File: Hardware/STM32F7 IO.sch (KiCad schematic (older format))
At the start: 33 parts, among them U4 STM32F765ZGT6, Y1 32.768kHz, Y2 8MHz

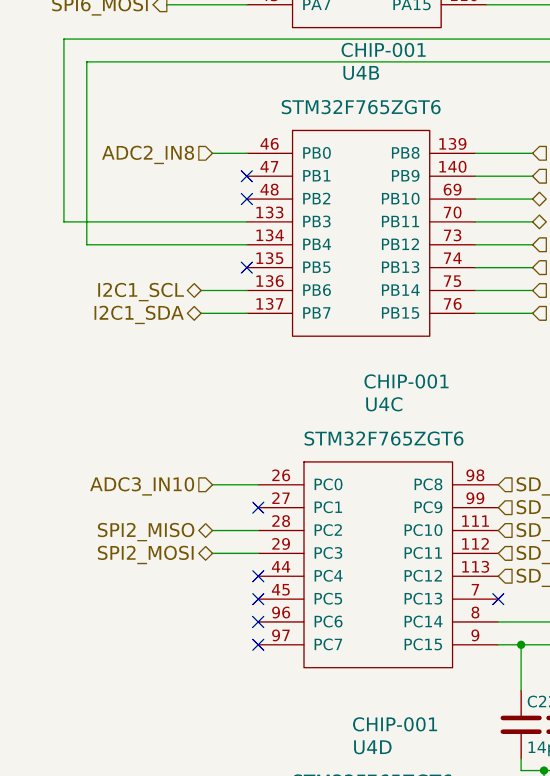
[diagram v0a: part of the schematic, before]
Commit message: Added additional headers to some interfaces, GPIOs, and FTDI pins. Added silks
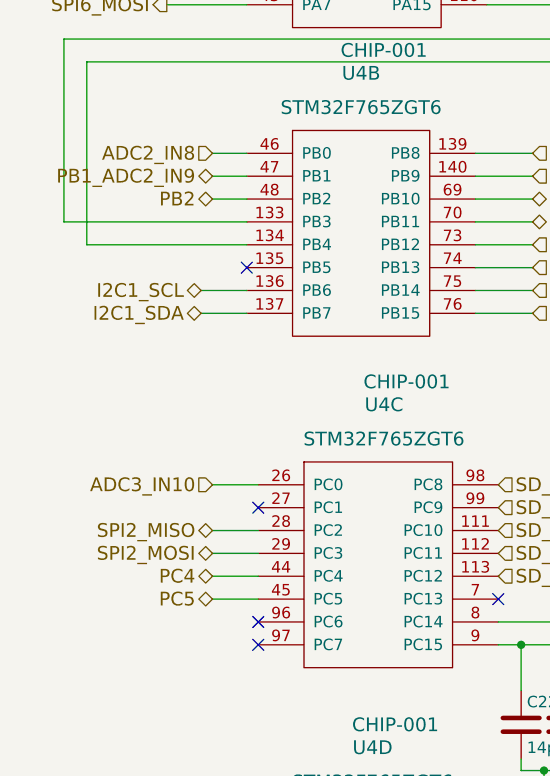
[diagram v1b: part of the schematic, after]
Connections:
- net PB1_ADC2_IN9: now reaches U4.47 (PB1)
- net PB2: now reaches U4.48 (PB2)
- net PC4: now reaches U4.44 (PC4)
- net PC5: now reaches U4.45 (PC5)
- no-connect marks 51 -> 47
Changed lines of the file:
@@
 $Descr A4 11693 8268
 encoding utf-8
-Sheet 3 10
+Sheet 10 10
 Title "Autopilot Controller I/O"
 Date "2017-05-14"
@@
 Text HLabel 7950 3200 2    60   BiDi ~ 0
 SPI5_NSS
-Text HLabel 1500 4600 0    60   BiDi ~ 0
-SPI2_MISO
-Text HLabel 1500 4700 0    60   BiDi ~ 0
-SPI2_MOSI
 Text HLabel 2900 3650 2    60   Input ~ 0
 UART4_CTS
@@
 MEM_WC
 NoConn ~ 1650 3450
-NoConn ~ 1650 3150
-NoConn ~ 1700 4800
-NoConn ~ 1700 4900
 NoConn ~ 2750 6200
 NoConn ~ 1700 6200
@@
 $Comp
 L WARG:STM32F765ZGT6 U4
-U 2 1 595F8A92
-P 2150 3500
-F 0 "U4" H 2150 4400 60  0000 C CNN
-F 1 "STM32F765ZGT6" H 2150 4250 60  0000 C CNN
-F 2 "Package_QFP:LQFP-144_20x20mm_P0.5mm" H 3200 3600 60  0001 C CNN
-F 3 "http://www.st.com/content/ccc/resource/technical/document/datasheet/group3/c5/37/9c/1d/a6/09/4e/1a/DM00273119/files/DM00273119.pdf/jcr:content/translations/en.DM00273119.pdf" H 3200 3600 60  0001 C CNN
-F 4 "CHIP-001" H 2250 4500 60  0000 C CNN "part_num"
-	2    2150 3500
-	1    0    0    -1
-$EndComp
-$Comp
-L WARG:STM32F765ZGT6 U4
-U 3 1 595F8B04
-P 2250 4950
-F 0 "U4" H 2250 5850 60  0000 C CNN
-F 1 "STM32F765ZGT6" H 2250 5700 60  0000 C CNN
-F 2 "Package_QFP:LQFP-144_20x20mm_P0.5mm" H 3300 5050 60  0001 C CNN
-F 3 "http://www.st.com/content/ccc/resource/technical/document/datasheet/group3/c5/37/9c/1d/a6/09/4e/1a/DM00273119/files/DM00273119.pdf/jcr:content/translations/en.DM00273119.pdf" H 3300 5050 60  0001 C CNN
-F 4 "CHIP-001" H 2350 5950 60  0000 C CNN "part_num"
-	3    2250 4950
-	1    0    0    -1
-$EndComp
-$Comp
-L WARG:STM32F765ZGT6 U4
 U 5 1 595F8BE2
 P 6500 2000
@@
 Wire Wire Line
 	1500 2950 1650 2950
-Wire Wire Line
-	1700 4700 1500 4700
-Wire Wire Line
-	1700 4600 1500 4600
 Wire Wire Line
 	5850 3500 6050 3500
@@
 	1300 2300 1650 2300
 NoConn ~ 1700 4500
-NoConn ~ 1650 3050
+$Comp
+L WARG:STM32F765ZGT6 U4
+U 3 1 595F8B04
+P 2250 4950
+F 0 "U4" H 2250 5850 60  0000 C CNN
+F 1 "STM32F765ZGT6" H 2250 5700 60  0000 C CNN
+F 2 "Package_QFP:LQFP-144_20x20mm_P0.5mm" H 3300 5050 60  0001 C CNN
+F 3 "http://www.st.com/content/ccc/resource/technical/document/datasheet/group3/c5/37/9c/1d/a6/09/4e/1a/DM00273119/files/DM00273119.pdf/jcr:content/translations/en.DM00273119.pdf" H 3300 5050 60  0001 C CNN
+F 4 "CHIP-001" H 2350 5950 60  0000 C CNN "part_num"
+	3    2250 4950
+	1    0    0    -1
+$EndComp
+Wire Wire Line
+	1700 4800 1500 4800
+Wire Wire Line
+	1500 4900 1700 4900
+$Comp
+L WARG:STM32F765ZGT6 U4
+U 2 1 595F8A92
+P 2150 3500
+F 0 "U4" H 2150 4400 60  0000 C CNN
+F 1 "STM32F765ZGT6" H 2150 4250 60  0000 C CNN
+F 2 "Package_QFP:LQFP-144_20x20mm_P0.5mm" H 3200 3600 60  0001 C CNN
+F 3 "http://www.st.com/content/ccc/resource/technical/document/datasheet/group3/c5/37/9c/1d/a6/09/4e/1a/DM00273119/files/DM00273119.pdf/jcr:content/translations/en.DM00273119.pdf" H 3200 3600 60  0001 C CNN
+F 4 "CHIP-001" H 2250 4500 60  0000 C CNN "part_num"
+	2    2150 3500
+	1    0    0    -1
+$EndComp
+Wire Wire Line
+	1650 3050 1500 3050
+Text HLabel 1500 4800 0    60   BiDi ~ 0
+PC4
+Text HLabel 1500 4900 0    60   BiDi ~ 0
+PC5
+Text HLabel 1500 3050 0    60   BiDi ~ 0
+PB1_ADC2_IN9
+Wire Wire Line
+	1650 3150 1500 3150
+Text HLabel 1500 3150 0    60   BiDi ~ 0
+PB2
+Wire Wire Line
+	1700 4600 1500 4600
+Wire Wire Line
+	1500 4700 1700 4700
+Text HLabel 1500 4600 0    60   BiDi ~ 0
+SPI2_MISO
+Text HLabel 1500 4700 0    60   BiDi ~ 0
+SPI2_MOSI
 $EndSCHEMATC

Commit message: associated components to their JLC part numbers
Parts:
- C22, C23: LCSC (none) -> C1644
- C24, C25, C26, C27, C28, C29, C30, C31, C33, C34, C35, C36: LCSC (none) -> C14663
- C32, C37: LCSC (none) -> C15849
- C38: LCSC (none) -> C19666
- C39, C40: LCSC (none) -> C1679
- C41, C42: LCSC (none) -> C23630
- D5, D6, D7: LCSC (none) -> C72043
- R16, R17, R18: LCSC (none) -> C22775
- R19: LCSC (none) -> C25804
- R20: LCSC (none) -> C21189
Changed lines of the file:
@@
 EESchema Schematic File Version 4
-LIBS:ZP-Breakout-cache
-EELAYER 29 0
+EELAYER 30 0
 EELAYER END
 $Descr A4 11693 8268
@@
 F 3 "https://ds.yuden.co.jp/TYCOMPAS/ut/specSheet?pn=TMK107ABJ225KA-T++" H 10350 5550 50  0001 C CNN
 F 4 "CAPP-007" H 10350 5550 60  0001 C CNN "part_num"
+F 5 "C23630" H 10350 5550 50  0001 C CNN "LCSC"
 	1    10350 5550
 	0    1    1    0
@@
 F 3 "https://ds.yuden.co.jp/TYCOMPAS/ut/specSheet?pn=TMK107ABJ225KA-T++" H 10350 5850 50  0001 C CNN
 F 4 "CAPP-007" H 10350 5850 60  0001 C CNN "part_num"
+F 5 "C23630" H 10350 5850 50  0001 C CNN "LCSC"
 	1    10350 5850
 	0    1    1    0
@@
 F 3 "https://search.murata.co.jp/Ceramy/image/img/A01X/G101/ENG/GRM188R71E104KA01-01.pdf" H 6350 4950 50  0001 C CNN
 F 4 "CAPP-005" H 6350 4950 60  0001 C CNN "part_num"
+F 5 "C14663" H 6350 4950 50  0001 C CNN "LCSC"
 	1    6350 4950
 	1    0    0    -1
@@
 F 3 "http://www.samsungsem.com/kr/support/product-search/mlcc/CL10A475MP5LNNC.jsp" H 8300 4950 50  0001 C CNN
 F 4 "CAPP-006" H 8300 4950 60  0001 C CNN "part_num"
+F 5 "C19666" H 8300 4950 50  0001 C CNN "LCSC"
 	1    8300 4950
 	1    0    0    1
@@
 F 3 "https://search.murata.co.jp/Ceramy/image/img/A01X/G101/ENG/GRM188R61E105KA12-01.pdf" H 7400 5700 50  0001 C CNN
 F 4 "CAPP-004" H 7400 5700 60  0001 C CNN "part_num"
+F 5 "C15849" H 7400 5700 50  0001 C CNN "LCSC"
 	1    7400 5700
 	1    0    0    1
@@
 F 3 "http://optoelectronics.liteon.com/upload/download/DS22-2000-228/LTST-C191KGKT.PDF" H 7850 1900 50  0001 C CNN
 F 4 "DIOD-002" H 7850 1900 60  0001 C CNN "part_num"
+F 5 "C72043" H 7850 1900 50  0001 C CNN "LCSC"
 	1    7850 1900
 	0    -1   -1   0
@@
 F 3 "http://optoelectronics.liteon.com/upload/download/DS22-2000-228/LTST-C191KGKT.PDF" H 8100 1900 50  0001 C CNN
 F 4 "DIOD-002" H 8100 1900 60  0001 C CNN "part_num"
+F 5 "C72043" H 8100 1900 50  0001 C CNN "LCSC"
 	1    8100 1900
 	0    -1   -1   0
@@
 F 3 "http://optoelectronics.liteon.com/upload/download/DS22-2000-228/LTST-C191KGKT.PDF" H 7600 1900 50  0001 C CNN
 F 4 "DIOD-002" H 7600 1900 60  0001 C CNN "part_num"
+F 5 "C72043" H 7600 1900 50  0001 C CNN "LCSC"
 	1    7600 1900
 	0    -1   -1   0
@@
 F 3 "http://www.yageo.com/documents/recent/PYu-RC_Group_51_RoHS_L_10.pdf" H 7600 2250 50  0001 C CNN
 F 4 "RESS-006" V 7600 2250 60  0001 C CNN "part_num"
+F 5 "C22775" V 7600 2250 50  0001 C CNN "LCSC"
 	1    7600 2250
 	1    0    0    -1
@@
 F 3 "http://www.yageo.com/documents/recent/PYu-RC_Group_51_RoHS_L_10.pdf" H 7850 2250 50  0001 C CNN
 F 4 "RESS-006" V 7850 2250 60  0001 C CNN "part_num"
+F 5 "C22775" V 7850 2250 50  0001 C CNN "LCSC"
 	1    7850 2250
 	1    0    0    -1
@@
 F 3 "http://www.yageo.com/documents/recent/PYu-RC_Group_51_RoHS_L_10.pdf" H 8100 2250 50  0001 C CNN
 F 4 "RESS-006" V 8100 2250 60  0001 C CNN "part_num"
+F 5 "C22775" V 8100 2250 50  0001 C CNN "LCSC"
 	1    8100 2250
 	1    0    0    -1
@@
 F 3 "https://search.murata.co.jp/Ceramy/image/img/A01X/G101/ENG/GRM188R61E105KA12-01.pdf" H 8100 5900 50  0001 C CNN
 F 4 "CAPP-004" H 8100 5900 60  0001 C CNN "part_num"
+F 5 "C15849" H 8100 5900 50  0001 C CNN "LCSC"
 	1    8100 5900
 	1    0    0    1
@@
 F 3 "https://search.murata.co.jp/Ceramy/image/img/A01X/G101/ENG/GRM188R71E104KA01-01.pdf" H 7800 5900 50  0001 C CNN
 F 4 "CAPP-005" H 7800 5900 60  0001 C CNN "part_num"
+F 5 "C14663" H 7800 5900 50  0001 C CNN "LCSC"
 	1    7800 5900
 	1    0    0    -1
@@
 F 3 "https://search.murata.co.jp/Ceramy/image/img/A01X/G101/ENG/GRM188R71E104KA01-01.pdf" H 7100 5700 50  0001 C CNN
 F 4 "CAPP-005" H 7100 5700 60  0001 C CNN "part_num"
+F 5 "C14663" H 7100 5700 50  0001 C CNN "LCSC"
 	1    7100 5700
 	1    0    0    -1
@@
 F 3 "https://search.murata.co.jp/Ceramy/image/img/A01X/G101/ENG/GRM188R71E104KA01-01.pdf" H 6550 4950 50  0001 C CNN
 F 4 "CAPP-005" H 6550 4950 60  0001 C CNN "part_num"
+F 5 "C14663" H 6550 4950 50  0001 C CNN "LCSC"
 	1    6550 4950
 	1    0    0    -1
@@
 F 3 "https://search.murata.co.jp/Ceramy/image/img/A01X/G101/ENG/GRM188R71E104KA01-01.pdf" H 6750 4950 50  0001 C CNN
 F 4 "CAPP-005" H 6750 4950 60  0001 C CNN "part_num"
+F 5 "C14663" H 6750 4950 50  0001 C CNN "LCSC"
 	1    6750 4950
 	1    0    0    -1
@@
 F 3 "https://search.murata.co.jp/Ceramy/image/img/A01X/G101/ENG/GRM188R71E104KA01-01.pdf" H 6950 4950 50  0001 C CNN
 F 4 "CAPP-005" H 6950 4950 60  0001 C CNN "part_num"
+F 5 "C14663" H 6950 4950 50  0001 C CNN "LCSC"
 	1    6950 4950
 	1    0    0    -1
@@
 F 3 "https://search.murata.co.jp/Ceramy/image/img/A01X/G101/ENG/GRM188R71E104KA01-01.pdf" H 7150 4950 50  0001 C CNN
 F 4 "CAPP-005" H 7150 4950 60  0001 C CNN "part_num"
+F 5 "C14663" H 7150 4950 50  0001 C CNN "LCSC"
 	1    7150 4950
 	1    0    0    -1
@@
 F 3 "https://search.murata.co.jp/Ceramy/image/img/A01X/G101/ENG/GRM188R71E104KA01-01.pdf" H 7350 4950 50  0001 C CNN
 F 4 "CAPP-005" H 7350 4950 60  0001 C CNN "part_num"
+F 5 "C14663" H 7350 4950 50  0001 C CNN "LCSC"
 	1    7350 4950
 	1    0    0    -1
@@
 F 3 "https://search.murata.co.jp/Ceramy/image/img/A01X/G101/ENG/GRM188R71E104KA01-01.pdf" H 7550 4950 50  0001 C CNN
 F 4 "CAPP-005" H 7550 4950 60  0001 C CNN "part_num"
+F 5 "C14663" H 7550 4950 50  0001 C CNN "LCSC"
 	1    7550 4950
 	1    0    0    -1
@@
 F 3 "https://search.murata.co.jp/Ceramy/image/img/A01X/G101/ENG/GRM188R71E104KA01-01.pdf" H 7750 4950 50  0001 C CNN
 F 4 "CAPP-005" H 7750 4950 60  0001 C CNN "part_num"
+F 5 "C14663" H 7750 4950 50  0001 C CNN "LCSC"
 	1    7750 4950
 	1    0    0    -1
@@
 F 3 "https://search.murata.co.jp/Ceramy/image/img/A01X/G101/ENG/GRM188R71E104KA01-01.pdf" H 7950 4950 50  0001 C CNN
 F 4 "CAPP-005" H 7950 4950 60  0001 C CNN "part_num"
+F 5 "C14663" H 7950 4950 50  0001 C CNN "LCSC"
 	1    7950 4950
 	1    0    0    -1
@@
 F 3 "http://www.yageo.com/documents/recent/PYu-RC_Group_51_RoHS_L_10.pdf" H 10550 3000 50  0001 C CNN
 F 4 "RESS-001" V 10550 3000 60  0001 C CNN "part_num"
+F 5 "C21189" V 10550 3000 50  0001 C CNN "LCSC"
 	1    10550 3000
 	0    1    1    0
@@
 F 3 "https://katalog.we-online.de/pbs/datasheet/885012006031.pdf" H 9000 3200 50  0001 C CNN
 F 4 "CAPP-009" H 9000 3200 60  0001 C CNN "part_num"
+F 5 "C1679" H 9000 3200 50  0001 C CNN "LCSC"
 	1    9000 3200
 	1    0    0    -1
@@
 F 3 "https://katalog.we-online.de/pbs/datasheet/885012006031.pdf" H 8800 3200 50  0001 C CNN
 F 4 "CAPP-009" H 8800 3200 60  0001 C CNN "part_num"
+F 5 "C1679" H 8800 3200 50  0001 C CNN "LCSC"
 	1    8800 3200
 	1    0    0    -1
@@
 F 3 "https://katalog.we-online.de/pbs/datasheet/885012006033.pdf" H 3050 5450 50  0001 C CNN
 F 4 "CAPP-008" H 3050 5450 60  0001 C CNN "part_num"
+F 5 "C1644" H 3050 5450 50  0001 C CNN "LCSC"
 	1    3050 5450
 	1    0    0    -1
@@
 F 3 "https://katalog.we-online.de/pbs/datasheet/885012006033.pdf" H 2850 5450 50  0001 C CNN
 F 4 "CAPP-008" H 2850 5450 60  0001 C CNN "part_num"
+F 5 "C1644" H 2850 5450 50  0001 C CNN "LCSC"
 	1    2850 5450
 	1    0    0    -1
@@
 F 3 "https://search.murata.co.jp/Ceramy/image/img/A01X/G101/ENG/GRM188R71E104KA01-01.pdf" H 6100 4950 50  0001 C CNN
 F 4 "CAPP-005" H 6100 4950 60  0001 C CNN "part_num"
+F 5 "C14663" H 6100 4950 50  0001 C CNN "LCSC"
 	1    6100 4950
 	1    0    0    -1
@@
 F 3 "http://www.yageo.com/documents/recent/PYu-RC_Group_51_RoHS_L_10.pdf" H 10250 3250 50  0001 C CNN
 F 4 "RESS-005" V 10250 3250 60  0001 C CNN "part_num"
+F 5 "C25804" V 10250 3250 50  0001 C CNN "LCSC"
 	1    10250 3250
 	-1   0    0    1
